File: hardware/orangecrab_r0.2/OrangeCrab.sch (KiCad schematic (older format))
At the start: 4 parts

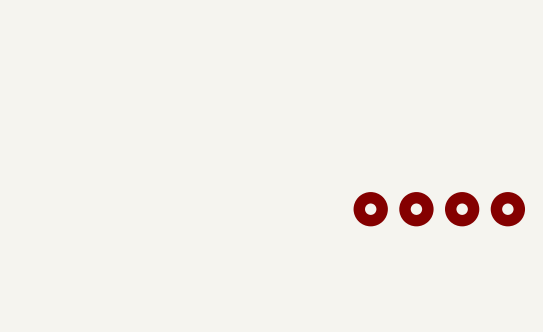
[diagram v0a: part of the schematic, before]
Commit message: hw: Update fiducials Add pullup to FLASH CS/SCK line Update BOM part numbers Fix Button pull-up voltage
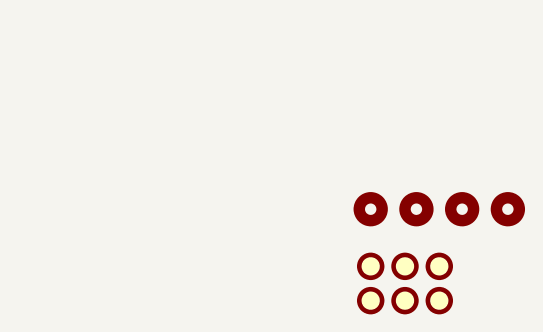
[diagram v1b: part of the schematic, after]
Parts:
- added FID1, FID2, FID3, FID4, FID5, FID6: Fiducial, Fiducial:Fiducial_0.75mm_Mask1.5mm, symbol Mechanical:Fiducial
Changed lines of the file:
@@
 F1 "decopling.sch" 50
 $EndSheet
+$Comp
+L Mechanical:Fiducial FID1
+U 1 1 5EA1EE5B
+P 10450 6650
+F 0 "FID1" H 10535 6696 50  0001 L CNN
+F 1 "Fiducial" H 10535 6605 50  0001 L CNN
+F 2 "Fiducial:Fiducial_0.75mm_Mask1.5mm" H 10450 6650 50  0001 C CNN
+F 3 "~" H 10450 6650 50  0001 C CNN
+	1    10450 6650
+	1    0    0    -1
+$EndComp
+$Comp
+L Mechanical:Fiducial FID2
+U 1 1 5EA1F2D2
+P 10600 6650
+F 0 "FID2" H 10685 6696 50  0001 L CNN
+F 1 "Fiducial" H 10685 6605 50  0001 L CNN
+F 2 "Fiducial:Fiducial_0.75mm_Mask1.5mm" H 10600 6650 50  0001 C CNN
+F 3 "~" H 10600 6650 50  0001 C CNN
+	1    10600 6650
+	1    0    0    -1
+$EndComp
+$Comp
+L Mechanical:Fiducial FID4
+U 1 1 5EA1F5F9
+P 10450 6800
+F 0 "FID4" H 10535 6846 50  0001 L CNN
+F 1 "Fiducial" H 10535 6755 50  0001 L CNN
+F 2 "Fiducial:Fiducial_0.75mm_Mask1.5mm" H 10450 6800 50  0001 C CNN
+F 3 "~" H 10450 6800 50  0001 C CNN
+	1    10450 6800
+	1    0    0    -1
+$EndComp
+$Comp
+L Mechanical:Fiducial FID5
+U 1 1 5EA1F603
+P 10600 6800
+F 0 "FID5" H 10685 6846 50  0001 L CNN
+F 1 "Fiducial" H 10685 6755 50  0001 L CNN
+F 2 "Fiducial:Fiducial_0.75mm_Mask1.5mm" H 10600 6800 50  0001 C CNN
+F 3 "~" H 10600 6800 50  0001 C CNN
+	1    10600 6800
+	1    0    0    -1
+$EndComp
+$Comp
+L Mechanical:Fiducial FID3
+U 1 1 5EA1FF05
+P 10750 6650
+F 0 "FID3" H 10835 6696 50  0001 L CNN
+F 1 "Fiducial" H 10835 6605 50  0001 L CNN
+F 2 "Fiducial:Fiducial_0.75mm_Mask1.5mm" H 10750 6650 50  0001 C CNN
+F 3 "~" H 10750 6650 50  0001 C CNN
+	1    10750 6650
+	1    0    0    -1
+$EndComp
+$Comp
+L Mechanical:Fiducial FID6
+U 1 1 5EA1FF0F
+P 10750 6800
+F 0 "FID6" H 10835 6846 50  0001 L CNN
+F 1 "Fiducial" H 10835 6755 50  0001 L CNN
+F 2 "Fiducial:Fiducial_0.75mm_Mask1.5mm" H 10750 6800 50  0001 C CNN
+F 3 "~" H 10750 6800 50  0001 C CNN
+	1    10750 6800
+	1    0    0    -1
+$EndComp
 $EndSCHEMATC
